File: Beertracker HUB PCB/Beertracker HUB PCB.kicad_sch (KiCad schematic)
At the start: 16 parts, among them J1 Conn_01x08_Pin - RC522 RFID, J2 Conn_01x04_Pin - I2C LCD, J3 Conn_01x03_Socket - DHT11, SW1 SW_Push - minus, SW2 SW_Push - Plus, U1 ESP32_NODEMCU

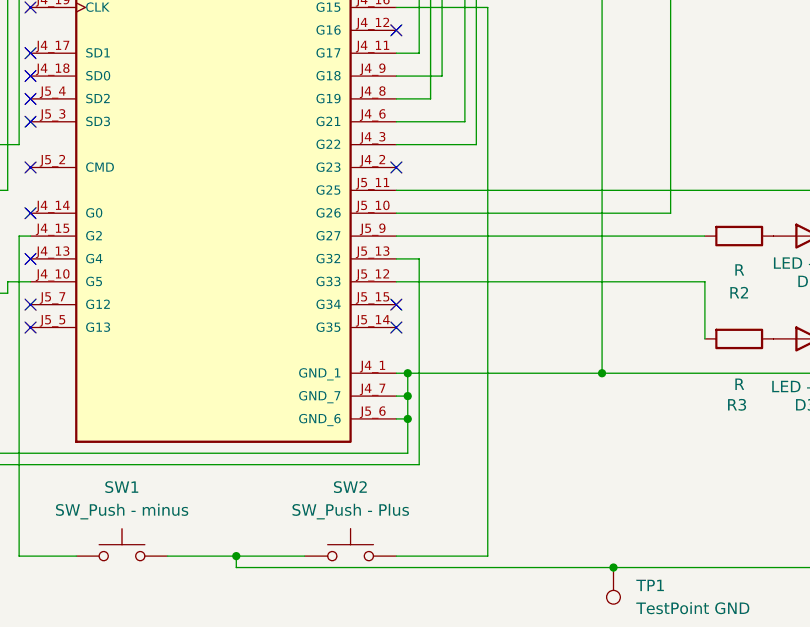
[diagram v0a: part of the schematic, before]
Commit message: finalized and ordered PCB design, changed code to be OLED screen orientated
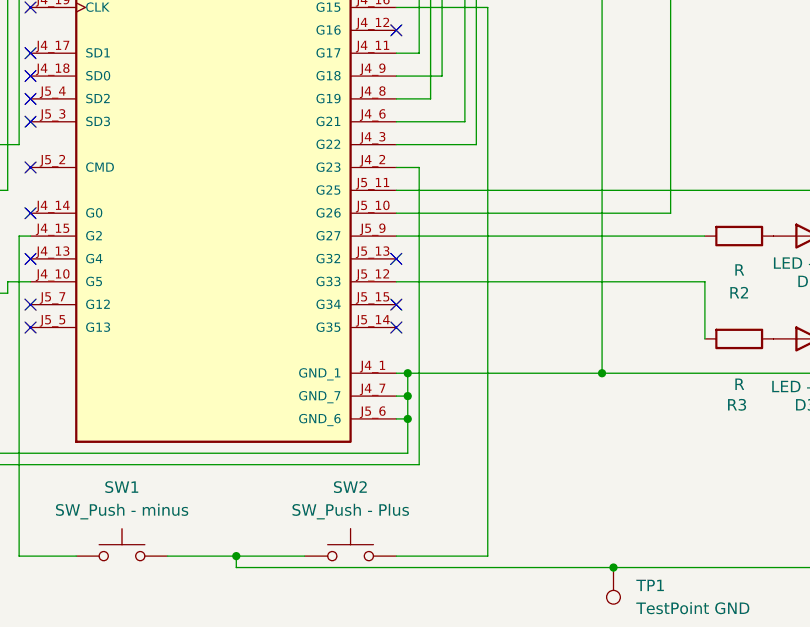
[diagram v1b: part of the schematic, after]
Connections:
- net at U1.J4_2 (G23): now also J1.3 (Pin_3)
- net at U1.J5_13 (G32): no longer J1.3 (Pin_3)
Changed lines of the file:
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@@
 		(title "Beertracker HUB PCB")
 		(date "30/12/2024")
-		(rev "1.0")
+		(rev "1.1")
 		(company "Beertracker")
 	)
@@
 	)
 	(no_connect
-		(at 102.87 76.2)
+		(at 102.87 86.36)
 	)
 	(wire
@@
 	(wire
 		(pts
-			(xy 105.41 109.22) (xy 105.41 86.36)
-		)
-		(stroke
-			(width 0)
-			(type default)
-		)
-	)
-	(wire
-		(pts
 			(xy 107.95 66.04) (xy 102.87 66.04)
 		)
@@
 	(wire
 		(pts
+			(xy 105.41 109.22) (xy 105.41 76.2)
+		)
+		(stroke
+			(width 0)
+			(type default)
+		)
+	)
+	(wire
+		(pts
+			(xy 54.61 109.22) (xy 105.41 109.22)
+		)
+		(stroke
+			(width 0)
+			(type default)
+		)
+	)
+	(wire
+		(pts
 			(xy 54.61 60.96) (xy 54.61 31.75)
 		)
@@
 	(wire
 		(pts
+			(xy 105.41 76.2) (xy 102.87 76.2)
+		)
+		(stroke
+			(width 0)
+			(type default)
+		)
+	)
+	(wire
+		(pts
 			(xy 104.14 43.18) (xy 102.87 43.18)
 		)
@@
 	(wire
 		(pts
-			(xy 54.61 109.22) (xy 105.41 109.22)
-		)
-		(stroke
-			(width 0)
-			(type default)
-		)
-	)
-	(wire
-		(pts
 			(xy 152.4 120.65) (xy 152.4 99.06)
 		)
@@
 	(wire
 		(pts
-			(xy 105.41 86.36) (xy 102.87 86.36)
+			(xy 54.61 76.2) (xy 54.61 109.22)
 		)
 		(stroke
@@
 		)
 		(stroke
-			(width 0)
-			(type default)
-		)
-	)
-	(wire
-		(pts
-			(xy 54.61 76.2) (xy 54.61 109.22)
-		)
-		(stroke
